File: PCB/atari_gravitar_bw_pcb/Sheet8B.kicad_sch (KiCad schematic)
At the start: 0 parts

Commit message: Worked on sheet 8B
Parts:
- added C136: 1000pf, symbol Device:C
- added C64, C66, C83, C84: .1, symbol Device:C
- added C65: .01, symbol Device:C
- added C72: .047, symbol Device:C
- added D_10: TL082, symbol atari:TL082
- added E_10: LF13201, symbol atari:LF13201
- added F_9: AM6012, symbol atari:AM6012
- added R83: 680, symbol Device:R_US
- added R84: 820, symbol Device:R_US
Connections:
- new net: C72.2, D_10.7, E_10.11
- new net: F_9.15 (VR-), R84.1
- new net: C65.1, R83.1
- new net: C65.2, R84.2
- new net +15V: C84.1, D_10.8 (V+)
- new net +5V: C64.2, F_9.20 (VCC)
- new net -15V: C66.1, C83.1, D_10.4 (V-), F_9.17 (V-)
- new net DVY10: F_9.4 (B4)
- new net DVY11: F_9.3 (B3)
- new net DVY3: F_9.11 (B11)
- new net DVY4: F_9.10 (B10)
- new net DVY5: F_9.9 (B9)
- new net DVY6: F_9.8 (B8)
- new net DVY7: F_9.7 (B7)
- new net DVY8: F_9.6 (B6)
- new net DVY9: F_9.5 (B5)
- new net GND: C136.2, C64.1, C66.2, C83.2, C84.2, D_10.5 (+), F_9.1 (B1), F_9.12 (B12), F_9.13 (GND), F_9.19 (~{IO})
- new net YBIP: C136.1, C72.1, D_10.6 (-), E_10.10, F_9.18 (IO)
- new net YREF: F_9.14 (VR+), R83.2
- new net ~{CENTER}: E_10.9
- new net ~{DVY12}: F_9.2 (B2)
- no-connect marks 0 -> 1

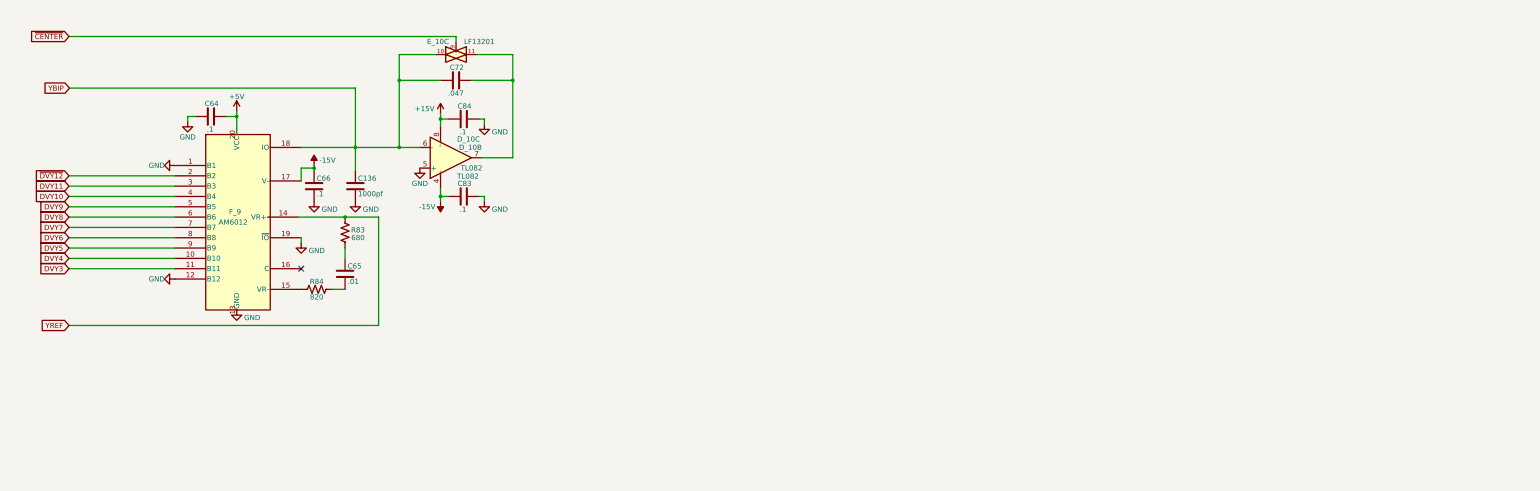
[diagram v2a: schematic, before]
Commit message: Completed sheet 8B
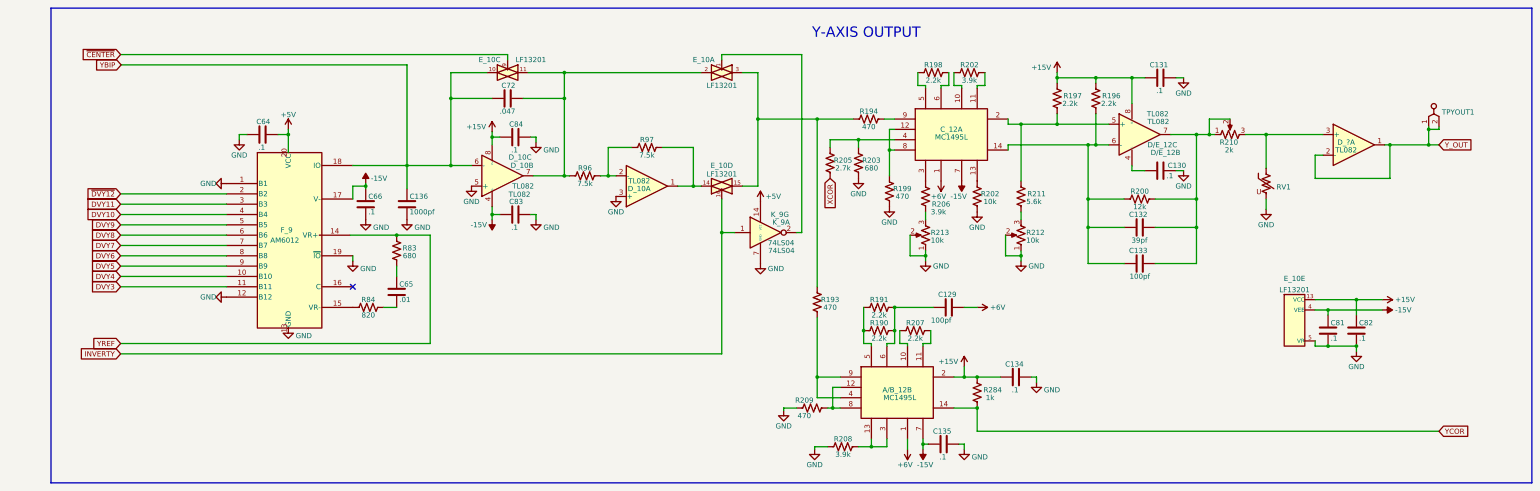
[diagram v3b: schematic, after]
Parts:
- added A/B_12, C_12: MC1495L, symbol atari:MC1495L
- added C129, C133: 100pf, symbol Device:C
- added C130, C131, C134, C135, C81, C82: .1, symbol Device:C
- added C132: 39pf, symbol Device:C
- added D/E_12, D_?: TL082, symbol atari:TL082
- added unit 1 of D_10
- added unit 5 of E_10
- added unit 1 of E_10
- added unit 4 of E_10
- added K_9: 74LS04, symbol atari:74LS04
- added R190, R191, R196, R197, R198, R207: 2.2k, symbol Device:R_US
- added R193, R194, R199, R209: 470, symbol Device:R_US
- added R200: 12k, symbol Device:R_US
- added R202: 10k, symbol Device:R_US
- added R202, R206, R208: 3.9k, symbol Device:R_US
- added R203: 680, symbol Device:R_US
- added R205: 2.7k, symbol Device:R_US
- added R210: 2k, symbol Device:R_Potentiometer_US
- added R211: 5.6k, symbol Device:R_US
- added R212, R213: 10k, symbol Device:R_Potentiometer_US
- added R284: 1k, symbol Device:R_US
- added R96, R97: 7.5k, symbol Device:R_US
- added RV1: Varistor_US, symbol Device:Varistor_US
- added TPYOUT1: tp_2_pin, symbol atari:tp_2_pin
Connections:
- net +15V: now also A/B_12.2, C131.1, C134.1, C82.1, D/E_12.8 (V+), E_10.13 (VCC), R196.2, R197.2, R284.2
- net +5V: now also K_9.14 (VCC)
- net -15V: now also A/B_12.7, C135.1, C81.1, C_12.7, E_10.4 (VEE)
- net GND: now also C130.2, C131.2, C134.2, C135.2, C81.2, C82.2, D_10.3 (+), E_10.5 (VR), K_9.7 (GND), R199.1, R202.1, R203.1, R208.1, R209.1, R212.1, R212.2, R213.1, R213.2, RV1.2
- net at C72.2, D_10.7, E_10.11: now also E_10.2, R96.1
- new net: C132.2, C133.2, D/E_12.7, R200.2, R210.1, R210.2
- new net: D_?.3 (+), R210.3, RV1.1
- new net: C_12.2, D/E_12.5 (+), R197.1, R211.2
- new net: C132.1, C133.1, C_12.14, D/E_12.6 (-), R196.1, R200.1
- new net: A/B_12.12, A/B_12.8, R209.2
- new net: R211.1, R212.3
- new net: C_12.13, R202.2
- new net: C_12.4, R203.2, R205.2
- new net: A/B_12.4, A/B_12.9, R193.1
- new net: E_10.15, E_10.3, R193.2, R194.1
- new net: C_12.10, R202.1
- new net: C_12.11, R202.2
- new net: C_12.12, C_12.8, R199.2
- new net: C_12.3, R206.2
- new net: C_12.5, R198.1
- new net: C_12.6, R198.2
- new net: C_12.9, R194.2
- new net: E_10.1, K_9.2
- new net: A/B_12.6, C129.1, R190.2, R191.2
- new net: A/B_12.13, A/B_12.3, R208.2
- new net: A/B_12.10, R207.1
- new net: A/B_12.11, R207.2
- new net: A/B_12.5, R190.1, R191.1
- new net: C130.1, D/E_12.4 (V-)
- new net: D_10.1, E_10.14, R97.2
- new net: R206.1, R213.3
- new net: D_10.2 (-), R96.2, R97.1
- new net +6V: A/B_12.1, C129.2, C_12.1
- new net INVERTY: E_10.16, K_9.1
- new net XCOR: R205.1
- new net YCOR: A/B_12.14, R284.1
- new net Y_OUT: D_?.1, D_?.2 (-), TPYOUT1.1, TPYOUT1.2
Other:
- note added: "Y-AXIS OUTPUT"
- moved on the sheet: C136, C64, C65, C66, C72, C83, C84, D_10B, D_10C, E_10C, F_9, R83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

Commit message: Completed sheet 8A
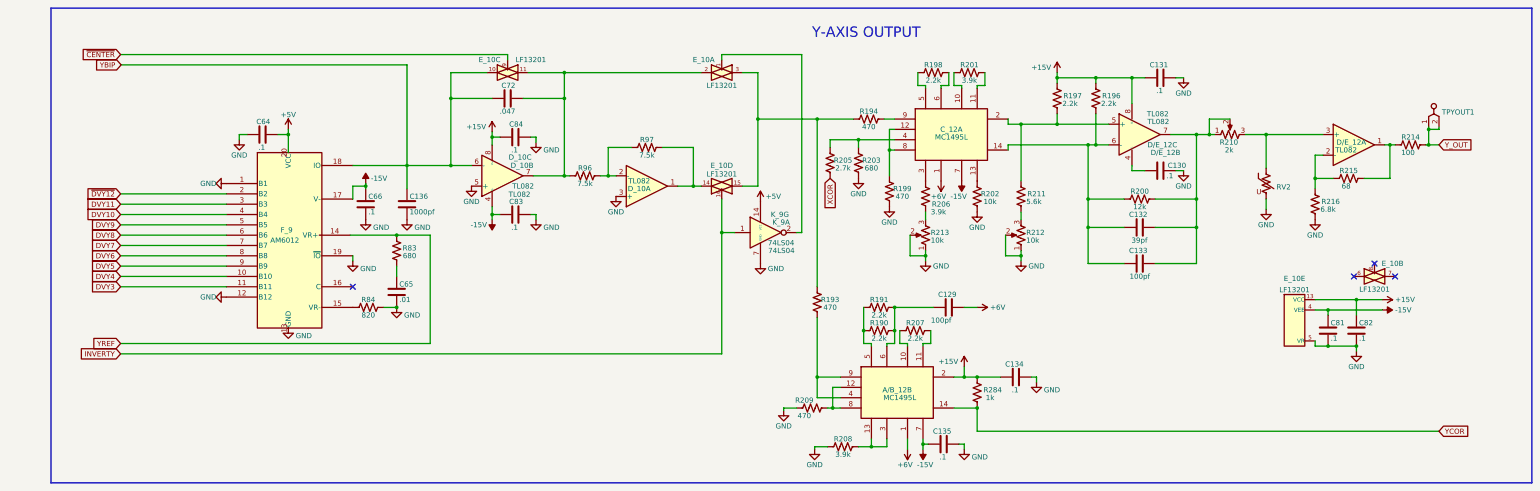
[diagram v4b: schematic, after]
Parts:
- added unit 2 of E_10
- added R214: 100, symbol Device:R_US
- added R215: 68, symbol Device:R_US
- added R216: 6.8k, symbol Device:R_US
- gave numbers to parts that had none: 1
- renumbered R202 to R201, RV1 to RV2
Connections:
- net GND: now also C65.2, R84.2, R216.1
- net Y_OUT: now also R214.1; no longer D/E_12.1, D/E_12.2 (-)
- new net: D/E_12.1, R214.2, R215.1
- new net: D/E_12.2 (-), R215.2, R216.2
- no-connect marks 1 -> 4
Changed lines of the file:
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@@
   (junction (at 246.38 180.34) (diameter 0) (color 0 0 0 0)
   )
+  (junction (at 346.075 156.21) (diameter 0) (color 0 0 0 0)
+  )
+  (junction (at 130.175 95.25) (diameter 0) (color 0 0 0 0)
+  )
+  (junction (at 259.715 171.45) (diameter 0) (color 0 0 0 0)
+  )
+  (junction (at 370.84 102.87) (diameter 0) (color 0 0 0 0)
+  )
+  (junction (at 220.345 100.33) (diameter 0) (color 0 0 0 0)
+  )
+  (junction (at 220.345 163.83) (diameter 0) (color 0 0 0 0)
+  )
+  (junction (at 353.06 156.21) (diameter 0) (color 0 0 0 0)
+  )
+  (junction (at 270.51 133.985) (diameter 0) (color 0 0 0 0)
+  )
+  (junction (at 247.015 133.985) (diameter 0) (color 0 0 0 0)
+  )
+  (junction (at 342.9 114.935) (diameter 0) (color 0 0 0 0)
+  )
+  (junction (at 287.02 127) (diameter 0) (color 0 0 0 0)
+  )
+  (junction (at 259.715 163.83) (diameter 0) (color 0 0 0 0)
+  )
+  (junction (at 270.51 101.6) (diameter 0) (color 0 0 0 0)
+  )
   (junction (at 370.84 106.68) (diameter 0) (color 0 0 0 0)
   )
-  (junction (at 346.075 156.21) (diameter 0) (color 0 0 0 0)
-  )
-  (junction (at 130.175 95.25) (diameter 0) (color 0 0 0 0)
-  )
-  (junction (at 259.715 171.45) (diameter 0) (color 0 0 0 0)
-  )
-  (junction (at 370.84 102.87) (diameter 0) (color 0 0 0 0)
-  )
-  (junction (at 220.345 100.33) (diameter 0) (color 0 0 0 0)
-  )
-  (junction (at 220.345 163.83) (diameter 0) (color 0 0 0 0)
-  )
-  (junction (at 353.06 156.21) (diameter 0) (color 0 0 0 0)
-  )
-  (junction (at 270.51 133.985) (diameter 0) (color 0 0 0 0)
-  )
-  (junction (at 247.015 133.985) (diameter 0) (color 0 0 0 0)
-  )
-  (junction (at 287.02 127) (diameter 0) (color 0 0 0 0)
-  )
-  (junction (at 259.715 163.83) (diameter 0) (color 0 0 0 0)
-  )
-  (junction (at 270.51 101.6) (diameter 0) (color 0 0 0 0)
-  )
   (junction (at 330.835 104.14) (diameter 0) (color 0 0 0 0)
   )
+  (junction (at 116.84 146.685) (diameter 0) (color 0 0 0 0)
+  )
   (junction (at 205.74 100.33) (diameter 0) (color 0 0 0 0)
   )
@@
   (junction (at 140.335 123.825) (diameter 0) (color 0 0 0 0)
   )
+  (junction (at 196.85 128.27) (diameter 0) (color 0 0 0 0)
+  )
+  (junction (at 313.69 127) (diameter 0) (color 0 0 0 0)
+  )
+  (junction (at 189.865 116.84) (diameter 0) (color 0 0 0 0)
+  )
+  (junction (at 316.865 104.14) (diameter 0) (color 0 0 0 0)
+  )
+  (junction (at 313.69 104.14) (diameter 0) (color 0 0 0 0)
+  )
+  (junction (at 116.84 128.905) (diameter 0) (color 0 0 0 0)
+  )
   (junction (at 361.315 106.68) (diameter 0) (color 0 0 0 0)
   )
-  (junction (at 196.85 128.27) (diameter 0) (color 0 0 0 0)
-  )
-  (junction (at 313.69 127) (diameter 0) (color 0 0 0 0)
-  )
-  (junction (at 189.865 116.84) (diameter 0) (color 0 0 0 0)
-  )
-  (junction (at 316.865 104.14) (diameter 0) (color 0 0 0 0)
-  )
-  (junction (at 313.69 104.14) (diameter 0) (color 0 0 0 0)
-  )
-  (junction (at 116.84 128.905) (diameter 0) (color 0 0 0 0)
-  )
   (junction (at 287.02 120.015) (diameter 0) (color 0 0 0 0)
   )
@@
   )
   (no_connect (at 106.045 141.605))
+  (no_connect (at 362.585 139.065))
+  (no_connect (at 357.505 135.89))
+  (no_connect (at 352.425 139.065))
   (wire (pts (xy 261.62 88.9) (xy 261.62 92.075))
     (stroke (width 0) (type default) (color 0 0 0 0))
@@
     (stroke (width 0) (type default) (color 0 0 0 0))
   )
+  (wire (pts (xy 361.315 106.68) (xy 362.585 106.68))
+    (stroke (width 0) (type default) (color 0 0 0 0))
+  )
   (wire (pts (xy 189.865 116.84) (xy 189.865 107.315))
     (stroke (width 0) (type default) (color 0 0 0 0))
@@
     (stroke (width 0) (type default) (color 0 0 0 0))
   )
+  (wire (pts (xy 342.9 114.935) (xy 347.345 114.935))
+    (stroke (width 0) (type default) (color 0 0 0 0))
+  )
   (wire (pts (xy 240.665 152.4) (xy 240.665 155.575))
     (stroke (width 0) (type default) (color 0 0 0 0))
@@
     (stroke (width 0) (type default) (color 0 0 0 0))
   )
+  (wire (pts (xy 342.9 114.935) (xy 342.9 117.475))
+    (stroke (width 0) (type default) (color 0 0 0 0))
+  )
   (wire (pts (xy 252.73 88.9) (xy 252.73 92.075))
     (stroke (width 0) (type default) (color 0 0 0 0))
@@
     (stroke (width 0) (type default) (color 0 0 0 0))
   )
+  (wire (pts (xy 370.205 106.68) (xy 370.84 106.68))
+    (stroke (width 0) (type default) (color 0 0 0 0))
+  )
   (wire (pts (xy 259.715 177.165) (xy 373.38 177.165))
     (stroke (width 0) (type default) (color 0 0 0 0))
@@
     (stroke (width 0) (type default) (color 0 0 0 0))
   )
+  (wire (pts (xy 354.965 114.935) (xy 361.315 114.935))
+    (stroke (width 0) (type default) (color 0 0 0 0))
+  )
   (wire (pts (xy 267.335 101.6) (xy 270.51 101.6))
     (stroke (width 0) (type default) (color 0 0 0 0))
@@
     (stroke (width 0) (type default) (color 0 0 0 0))
   )
-  (wire (pts (xy 342.9 114.935) (xy 361.315 114.935))
-    (stroke (width 0) (type default) (color 0 0 0 0))
-  )
   (wire (pts (xy 273.05 163.83) (xy 274.32 163.83))
     (stroke (width 0) (type default) (color 0 0 0 0))
@@
   )
   (wire (pts (xy 295.91 135.89) (xy 287.02 135.89))
-    (stroke (width 0) (type default) (color 0 0 0 0))
-  )
-  (wire (pts (xy 361.315 106.68) (xy 370.84 106.68))
     (stroke (width 0) (type default) (color 0 0 0 0))
   )
@@
     (pin "1")
   )
+  (symbol (lib_id "power:GND") (at 116.84 146.685 0) (unit 1)
+    (in_bom yes) (on_board yes)
+    (property "Reference" "#PWR0480" (id 0) (at 116.84 153.035 0)
+      (effects (font (size 1.27 1.27)) hide)
+    )
+    (property "Value" "GND" (id 1) (at 120.65 148.59 0))
+    (property "Footprint" "" (id 2) (at 116.84 146.685 0)
+      (effects (font (size 1.27 1.27)) hide)
+    )
+    (property "Datasheet" "" (id 3) (at 116.84 146.685 0)
+      (effects (font (size 1.27 1.27)) hide)
+    )
+    (pin "1")
+  )
   (symbol (lib_id "power:+6V") (at 250.825 115.57 180) (unit 1)
     (in_bom yes) (on_board yes)
@@
     (pin "2")
   )
+  (symbol (lib_id "atari:LF13201") (at 357.505 139.065 0) (unit 2)
+    (in_bom yes) (on_board yes)
+    (property "Reference" "E_10" (id 0) (at 361.95 135.89 0))
+    (property "Value" "LF13201" (id 1) (at 357.505 142.24 0))
+    (property "Footprint" "" (id 2) (at 357.505 139.065 0)
+      (effects (font (size 1.524 1.524)) hide)
+    )
+    (property "Datasheet" "" (id 3) (at 357.505 139.065 0)
+      (effects (font (size 1.524 1.524)) hide)
+    )
+    (pin "6")
+    (pin "7")
+    (pin "8")
+  )
   (symbol (lib_id "Device:R_US") (at 270.51 119.38 180) (unit 1)
     (in_bom yes) (on_board yes)
@@
     )
     (pin "1")
+  )
+  (symbol (lib_id "Device:R_US") (at 351.155 114.935 270) (unit 1)
+    (in_bom yes) (on_board yes)
+    (property "Reference" "R215" (id 0) (at 351.155 113.03 90))
+    (property "Value" "68" (id 1) (at 350.52 116.84 90))
+    (property "Footprint" "" (id 2) (at 350.901 115.951 90)
+      (effects (font (size 1.27 1.27)) hide)
+    )
+    (property "Datasheet" "~" (id 3) (at 351.155 114.935 0)
+      (effects (font (size 1.27 1.27)) hide)
+    )
+    (pin "1")
+    (pin "2")
   )
   (symbol (lib_id "power:-15V") (at 109.22 116.205 0) (unit 1)
@@
   (symbol (lib_id "atari:TL082") (at 352.425 106.68 0) (unit 1)
     (in_bom yes) (on_board yes)
-    (property "Reference" "D_?" (id 0) (at 350.52 106.045 0))
+    (property "Reference" "D/E_12" (id 0) (at 351.79 106.045 0))
     (property "Value" "TL082" (id 1) (at 350.52 107.95 0))
     (property "Footprint" "" (id 2) (at 352.425 106.68 0)
@@
   (symbol (lib_id "Device:Varistor_US") (at 330.835 116.205 0) (unit 1)
     (in_bom yes) (on_board yes) (fields_autoplaced)
-    (property "Reference" "RV1" (id 0) (at 333.375 117.0603 0)
+    (property "Reference" "RV2" (id 0) (at 333.375 117.0603 0)
       (effects (font (size 1.27 1.27)) (justify left))
     )
@@
   (symbol (lib_id "Device:R_US") (at 257.81 88.9 90) (unit 1)
     (in_bom yes) (on_board yes)
-    (property "Reference" "R202" (id 0) (at 257.81 86.995 90))
+    (property "Reference" "R201" (id 0) (at 257.81 86.995 90))
     (property "Value" "3.9k" (id 1) (at 257.81 90.805 90))
     (property "Footprint" "" (id 2) (at 258.064 87.884 90)
@@
     (pin "2")
   )
+  (symbol (lib_id "power:GND") (at 342.9 125.095 0) (unit 1)
+    (in_bom yes) (on_board yes)
+    (property "Reference" "#PWR0479" (id 0) (at 342.9 131.445 0)
+      (effects (font (size 1.27 1.27)) hide)
+    )
+    (property "Value" "GND" (id 1) (at 342.9 128.905 0))
+    (property "Footprint" "" (id 2) (at 342.9 125.095 0)
+      (effects (font (size 1.27 1.27)) hide)
+    )
+    (property "Datasheet" "" (id 3) (at 342.9 125.095 0)
+      (effects (font (size 1.27 1.27)) hide)
+    )
+    (pin "1")
+  )
   (symbol (lib_id "Device:C") (at 146.05 123.825 90) (unit 1)
     (in_bom yes) (on_board yes)
@@
     )
     (property "Datasheet" "~" (id 3) (at 146.05 104.775 0)
+      (effects (font (size 1.27 1.27)) hide)
+    )
+    (pin "1")
+    (pin "2")
+  )
+  (symbol (lib_id "Device:R_US") (at 342.9 121.285 180) (unit 1)
+    (in_bom yes) (on_board yes)
+    (property "Reference" "R216" (id 0) (at 346.71 120.65 0))
+    (property "Value" "6.8k" (id 1) (at 346.075 122.555 0))
+    (property "Footprint" "" (id 2) (at 341.884 121.031 90)
+      (effects (font (size 1.27 1.27)) hide)
+    )
+    (property "Datasheet" "~" (id 3) (at 342.9 121.285 0)
       (effects (font (size 1.27 1.27)) hide)
     )
@@
       (effects (font (size 1.27 1.27)) hide)
     )
+    (pin "1")
+    (pin "2")
+  )
+  (symbol (lib_id "Device:R_US") (at 366.395 106.68 270) (unit 1)
+    (in_bom yes) (on_board yes)
+    (property "Reference" "R214" (id 0) (at 366.395 104.775 90))
+    (property "Value" "100" (id 1) (at 365.76 108.585 90))
+    (property "Footprint" "" (id 2) (at 366.141 107.696 90)
+      (effects (font (size 1.27 1.27)) hide)
+    )
+    (property "Datasheet" "~" (id 3) (at 366.395 106.68 0)
+      (effects (font (size 1.27 1.27)) hide)
+    )
